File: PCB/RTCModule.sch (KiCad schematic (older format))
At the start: 27 parts, among them Q401 IRLML2502, Q402 IRLML2502, Q403 IRLML2502, Q404 IRLML2502, Q405 IRLML2502, Q406 IRLML2502, Q407 NOPOP, Q408 IRLML2502, U401 RTC-DCF77

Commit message: Completed draft layout for the alternate layout
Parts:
- removed TP1, TP2: CONN_01X06, Pin_Headers:Pin_Header_Straight_1x06, symbol CONN_01X06
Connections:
- wire segments 104 -> 87
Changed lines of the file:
@@
 	4050 950  5450 950
 Wire Wire Line
-	5350 600  5350 1100
-Wire Wire Line
 	5350 1100 5450 1100
-Connection ~ 5350 950
 Wire Wire Line
 	5800 2400 5800 2650
@@
 	6450 1400 6850 1400
 NoConn ~ 8100 5100
-$Comp
-L CONN_01X06 TP1
-U 1 1 55D23692
-P 9400 1350
-F 0 "TP1" H 9400 1700 50  0000 C CNN
-F 1 "CONN_01X06" V 9500 1350 50  0000 C CNN
-F 2 "Pin_Headers:Pin_Header_Straight_1x06" H 9400 1350 60  0001 C CNN
-F 3 "" H 9400 1350 60  0000 C CNN
-	1    9400 1350
-	1    0    0    -1
-$EndComp
-$Comp
-L CONN_01X06 TP2
-U 1 1 55D23781
-P 9450 2450
-F 0 "TP2" H 9450 2800 50  0000 C CNN
-F 1 "CONN_01X06" V 9550 2450 50  0000 C CNN
-F 2 "Pin_Headers:Pin_Header_Straight_1x06" H 9450 2450 60  0001 C CNN
-F 3 "" H 9450 2450 60  0000 C CNN
-	1    9450 2450
-	1    0    0    -1
-$EndComp
-Text GLabel 9000 1200 0    60   Input ~ 0
-~L_SS
-Text GLabel 9000 1300 0    60   Input ~ 0
-L_SCK
-Text GLabel 9000 1400 0    60   Input ~ 0
-L_MOSI
-Text GLabel 9000 1500 0    60   Input ~ 0
-L_MISO
-$Comp
-L GND #PWR402
-U 1 1 55D23BA4
-P 8900 1700
-F 0 "#PWR402" H 8900 1450 50  0001 C CNN
-F 1 "GND" H 8900 1550 50  0000 C CNN
-F 2 "" H 8900 1700 60  0000 C CNN
-F 3 "" H 8900 1700 60  0000 C CNN
-	1    8900 1700
-	1    0    0    -1
-$EndComp
-Wire Wire Line
-	9200 1600 8900 1600
-Wire Wire Line
-	8900 1600 8900 1700
-Wire Wire Line
-	9200 1500 9000 1500
-Wire Wire Line
-	9200 1400 9000 1400
-Wire Wire Line
-	9200 1300 9000 1300
-Wire Wire Line
-	9200 1200 9000 1200
-Text GLabel 9050 2300 0    60   Input ~ 0
-L_Periodic_INT
-Text GLabel 9050 2400 0    60   Input ~ 0
-L_DCF_RCPT
-Text GLabel 9050 2500 0    60   Input ~ 0
-L_Rx
-Text GLabel 9050 2600 0    60   Input ~ 0
-L_ALARM_INT
-$Comp
-L GND #PWR403
-U 1 1 55D24A11
-P 9050 2850
-F 0 "#PWR403" H 9050 2600 50  0001 C CNN
-F 1 "GND" H 9050 2700 50  0000 C CNN
-F 2 "" H 9050 2850 60  0000 C CNN
-F 3 "" H 9050 2850 60  0000 C CNN
-	1    9050 2850
-	1    0    0    -1
-$EndComp
-Wire Wire Line
-	9250 2700 9050 2700
-Wire Wire Line
-	9050 2700 9050 2850
-Wire Wire Line
-	9250 2600 9050 2600
-Wire Wire Line
-	9250 2500 9050 2500
-Wire Wire Line
-	9250 2400 9050 2400
-Wire Wire Line
-	9250 2300 9050 2300
-Wire Wire Line
-	9200 600  9200 1100
-Wire Wire Line
-	9750 600  9750 1950
-Wire Wire Line
-	9750 1950 9250 1950
-Wire Wire Line
-	9250 1950 9250 2200
-Connection ~ 9200 600
-Wire Wire Line
-	5350 600  9750 600
+Wire Wire Line
+	5350 1100 5350 950
+Connection ~ 5350 950
 $EndSCHEMATC

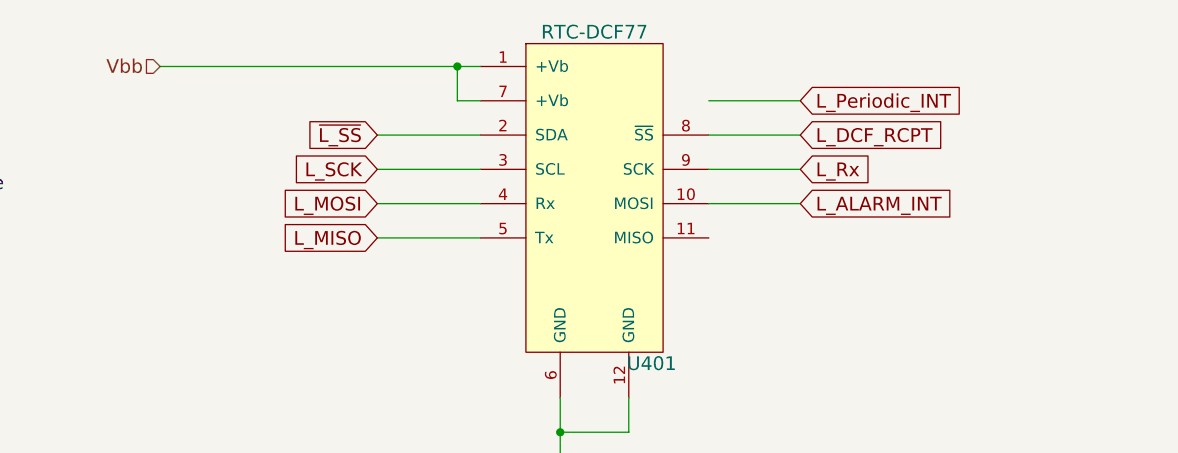
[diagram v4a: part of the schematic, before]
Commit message: Made corrections to the board for rev 2L.2
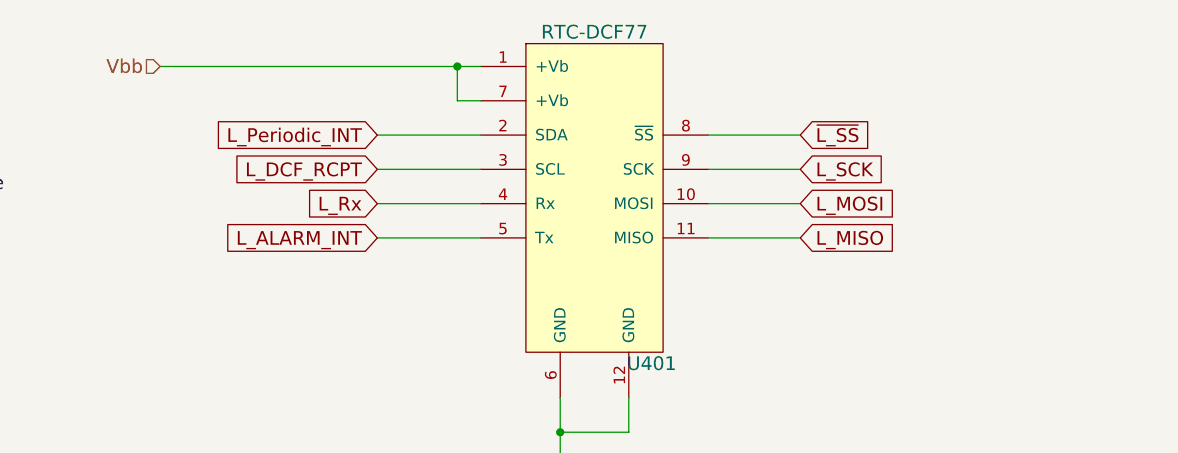
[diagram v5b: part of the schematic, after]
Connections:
- net L_ALARM_INT: now also U401.5 (Tx); no longer U401.10 (MOSI)
- net L_DCF_RCPT: now also U401.3 (SCL); no longer U401.8 (~SS)
- net L_MISO: now also U401.11 (MISO); no longer U401.5 (Tx)
- net L_MOSI: now also U401.10 (MOSI); no longer U401.4 (Rx)
- net L_Periodic_INT: now also U401.2 (SDA)
- net L_Rx: now also U401.4 (Rx); no longer U401.9 (SCK)
- net L_SCK: now also U401.9 (SCK); no longer U401.3 (SCL)
- net ~L_SS: now also U401.8 (~SS); no longer U401.2 (SDA)
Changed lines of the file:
@@
 Vbb
 $Comp
-L GND #PWR401
+L GND #PWR07
 U 1 1 5570847C
 P 5800 2650
-F 0 "#PWR401" H 5800 2400 50  0001 C CNN
+F 0 "#PWR07" H 5800 2400 50  0001 C CNN
 F 1 "GND" H 5800 2500 50  0000 C CNN
 F 2 "" H 5800 2650 60  0000 C CNN
@@
 Text GLabel 8350 4950 3    60   Input ~ 0
 L_ALARM_INT
-Text GLabel 5000 1700 0    60   Input ~ 0
+Text GLabel 6850 1700 2    60   Input ~ 0
 L_MISO
-Text GLabel 5000 1550 0    60   Input ~ 0
+Text GLabel 6850 1550 2    60   Input ~ 0
 L_MOSI
-Text GLabel 5000 1400 0    60   Input ~ 0
+Text GLabel 6850 1400 2    60   Input ~ 0
 L_SCK
-Text GLabel 5000 1250 0    60   Input ~ 0
+Text GLabel 6850 1250 2    60   Input ~ 0
 ~L_SS
 Text Notes 1250 1600 0    60   ~ 0
@@
 Wire Wire Line
 	6300 5750 9100 5750
-Text GLabel 6850 1100 2    60   Input ~ 0
+Text GLabel 5000 1250 0    60   Input ~ 0
 L_Periodic_INT
-Text GLabel 6850 1250 2    60   Input ~ 0
+Text GLabel 5000 1400 0    60   Input ~ 0
 L_DCF_RCPT
-Text GLabel 6850 1550 2    60   Input ~ 0
+Text GLabel 5000 1700 0    60   Input ~ 0
 L_ALARM_INT
 Wire Wire Line
-	6450 1100 6850 1100
-Wire Wire Line
 	6450 1250 6850 1250
 Wire Wire Line
 	6450 1550 6850 1550
-Text GLabel 6850 1400 2    60   Input ~ 0
+Text GLabel 5000 1550 0    60   Input ~ 0
 L_Rx
 Wire Wire Line
@@
 	5350 1100 5350 950
 Connection ~ 5350 950
+Wire Wire Line
+	6850 1700 6450 1700
 $EndSCHEMATC
